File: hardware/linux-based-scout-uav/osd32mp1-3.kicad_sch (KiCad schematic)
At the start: 0 parts

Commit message: Updates (Schematic, Readme, doc)
Updates to Schematic capture, README file and doc files.
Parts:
- added U1: OSD32MP157C-512M-IAA, OSD32MP157C-512M-IAA:OSD32MP15X-BGA-324, symbol OSD32MP157C-512M-IAA:OSD32MP157C-512M-IAA

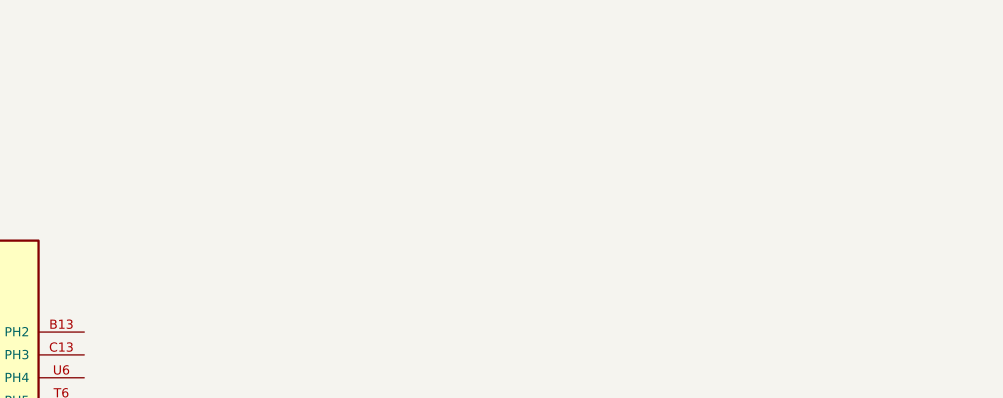
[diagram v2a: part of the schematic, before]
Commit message: Schematic updates
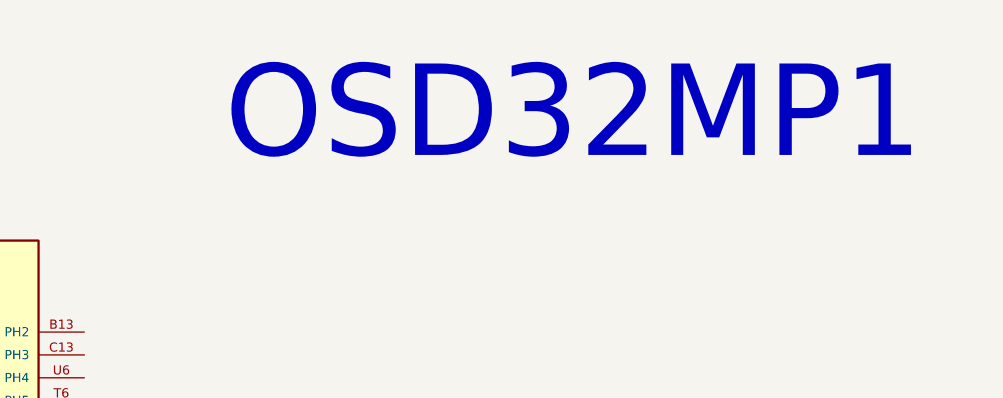
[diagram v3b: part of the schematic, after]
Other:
- note added: "OSD32MP1"
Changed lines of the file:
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@@
 	(generator_version "8.0")
 	(paper "A3")
+	(text "OSD32MP1"
+		(exclude_from_sim no)
+		(at 205.486 22.86 0)
+		(effects
+			(font
+				(size 10.16 10.16)
+			)
+		)
+	)
 	(symbol
 		(lib_id "OSD32MP157C-512M-IAA:OSD32MP157C-512M-IAA")

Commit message: Schematic/board update
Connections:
- net MMC2_D6: now reaches U1.V15 (PE5)
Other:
- note added: "MMC2_D[0..7] Bus"

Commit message: Schematic update
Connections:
- net MMC2_CLK: now reaches U1.T12 (PE3)
- net MMC2_CMD: now reaches U1.U15 (PG6)
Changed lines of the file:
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@@
+		)
+	)
+	(wire
+		(pts
+			(xy 67.31 153.67) (xy 90.17 153.67)
+		)
+		(stroke
+			(width 0)
+			(type default)
 		)
 	)
@@
 		(pts
 			(xy 49.53 247.65) (xy 66.04 247.65)
+		)
+		(stroke
+			(width 0)
+			(type default)
+		)
+	)
+	(wire
+		(pts
+			(xy 67.31 49.53) (xy 90.17 49.53)
 		)
 		(stroke
@@
 			)
 		)
+	)
+	(global_label "MMC2_CMD"
+		(shape input)
+		(at 67.31 153.67 180)
+		(fields_autoplaced yes)
+		(effects
+			(font
+				(size 1.27 1.27)
+			)
+			(justify right)
+		)
+		(property "Intersheetrefs" "${INTERSHEET_REFS}"
+			(at 53.9835 153.67 0)
+			(effects
+				(font
+					(size 1.27 1.27)
+				)
+				(justify right)
+				(hide yes)
+			)
+		)
+	)
+	(global_label "MMC2_CLK"
+		(shape input)
+		(at 67.31 49.53 180)
+		(fields_autoplaced yes)
+		(effects
+			(font
+				(size 1.27 1.27)
+			)
+			(justify right)
+		)
+		(property "Intersheetrefs" "${INTERSHEET_REFS}"
+			(at 54.4068 49.53 0)
+			(effects
+				(font
+					(size 1.27 1.27)
+				)
+				(justify right)
+				(hide yes)
+			)
+		)
